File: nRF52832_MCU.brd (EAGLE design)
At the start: 43.2 x 22.1 mm, 27 parts, among them J100 DEBUG_CONNECTOR, U1 NRF52832, X1 32MHz, X2 32.768kHz

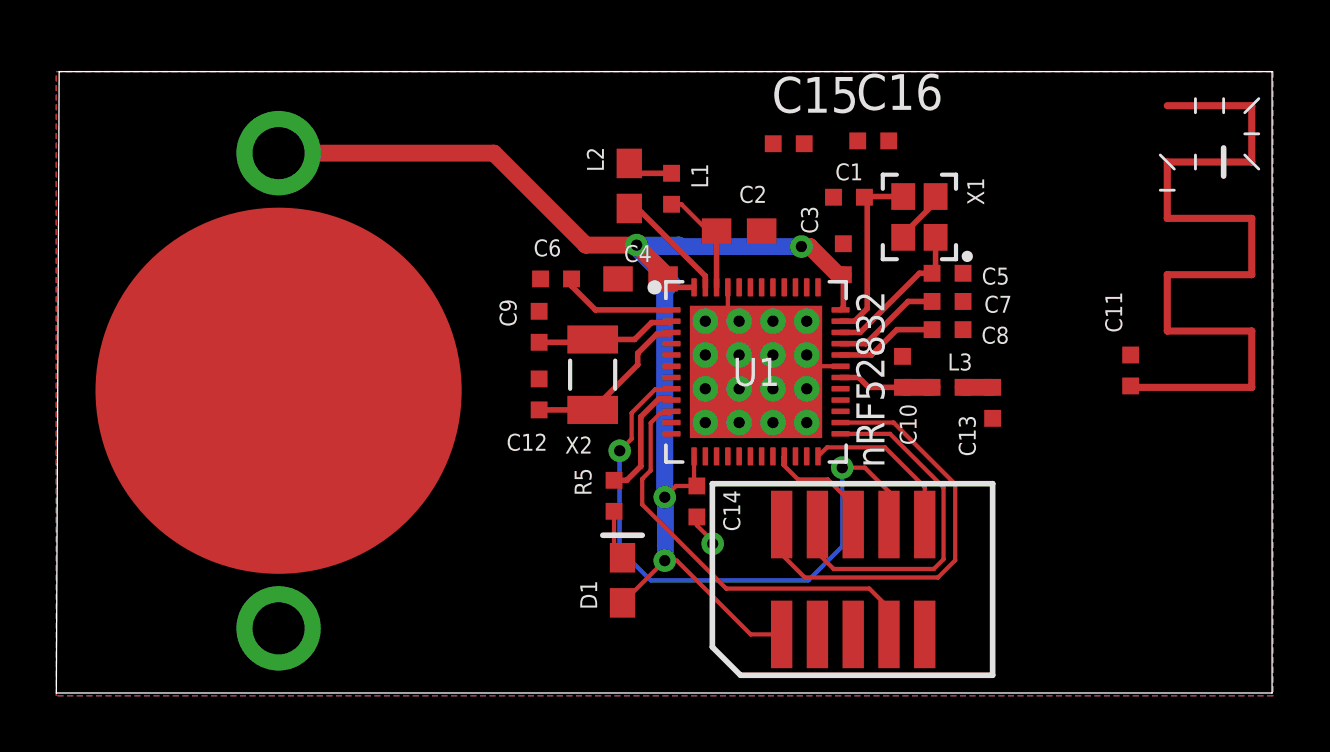
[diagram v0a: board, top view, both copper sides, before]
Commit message: Add missing capacitors
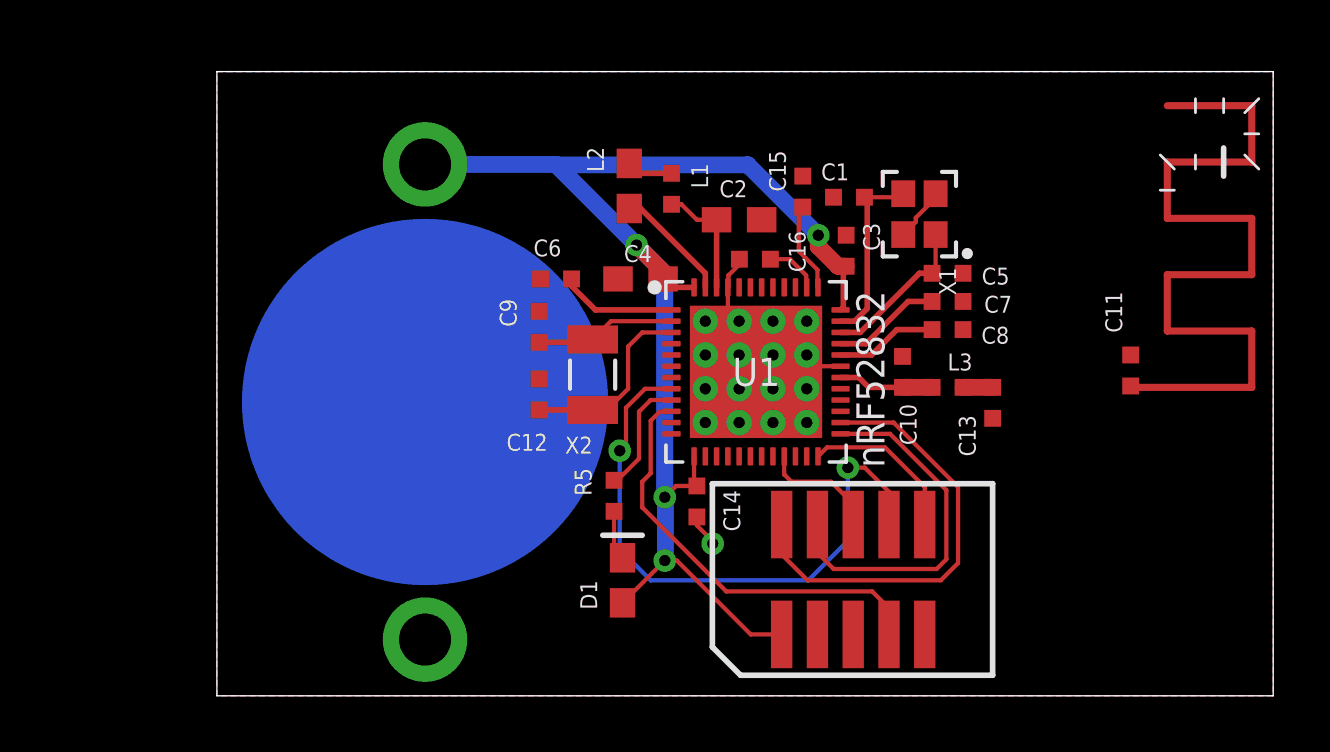
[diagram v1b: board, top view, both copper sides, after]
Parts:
- moved C16 5.94 mm to (37.3, 15.4), turned to 180 degrees
- moved BATT1 5.22 mm to (25.6, 10.3), flipped to the bottom
- moved C15 1.77 mm to (39.0, 17.8), turned to 90 degrees
- moved C2 0.40 mm to (36.7, 16.8)
- moved C3 0.32 mm to (40.5, 15.7)
- moved X1 0.10 mm to (43.1, 17.0)
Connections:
- removed net N$1: ANT1.P$1, C11.1
- net N$5: now also ANT1.P$1, C11.1
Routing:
- net P0.25: track 0.00 -> 3.19 mm
- net P0.26: track 0.00 -> 1.94 mm
- net VDD_P3V3: track 49.1 -> 50.6 mm
- net GND: track 7.28 -> 8.47 mm
- net XL2: track 6.08 -> 6.72 mm
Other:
- board size 43.2 x 22.1 mm -> 37.5 x 22.2 mm

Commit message: Update rastnest
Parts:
- moved C5 0.10 mm to (44.1, 15.0)
- moved C7 0.10 mm to (44.1, 14.0)
- moved C8 0.10 mm to (44.1, 13.0)
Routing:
- net VDD_P3V3: track 50.6 -> 47.1 mm
- net P0.06_TX: track 21.7 -> 20.2 mm

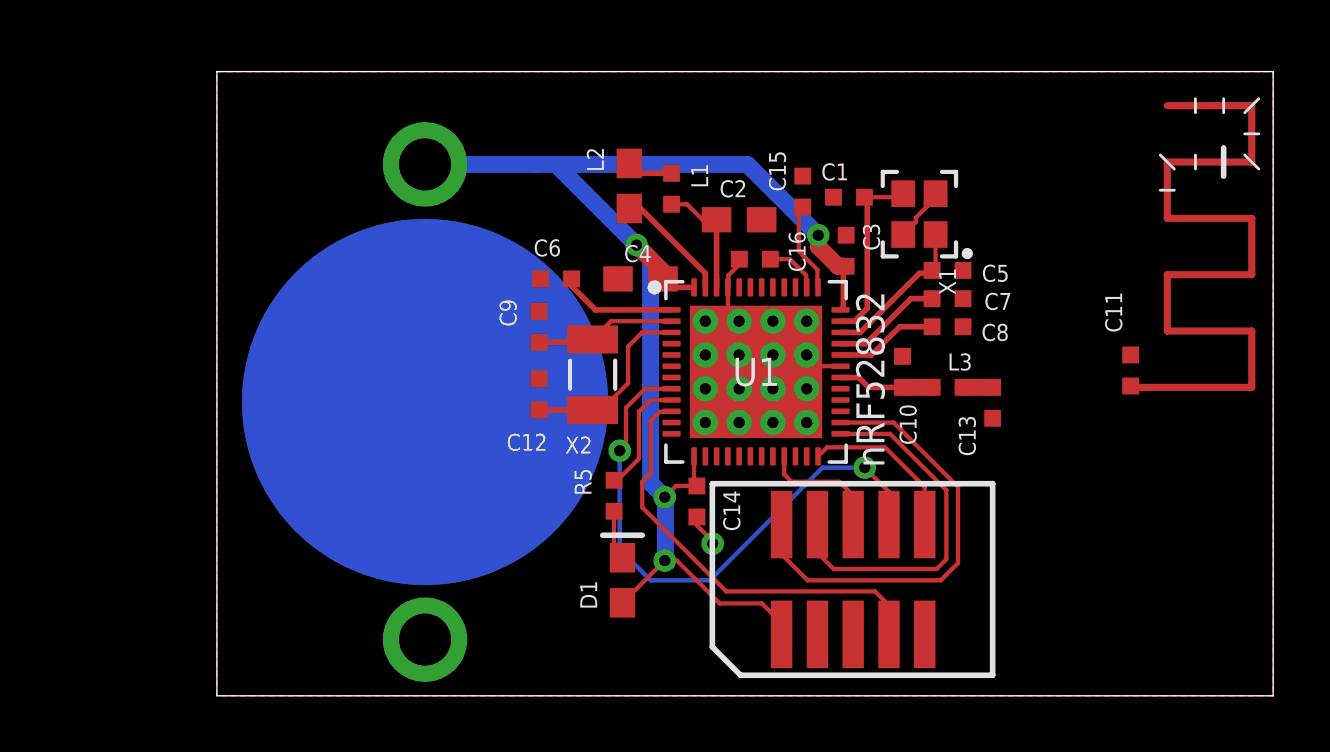
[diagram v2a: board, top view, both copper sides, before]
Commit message: Add additional pin connector
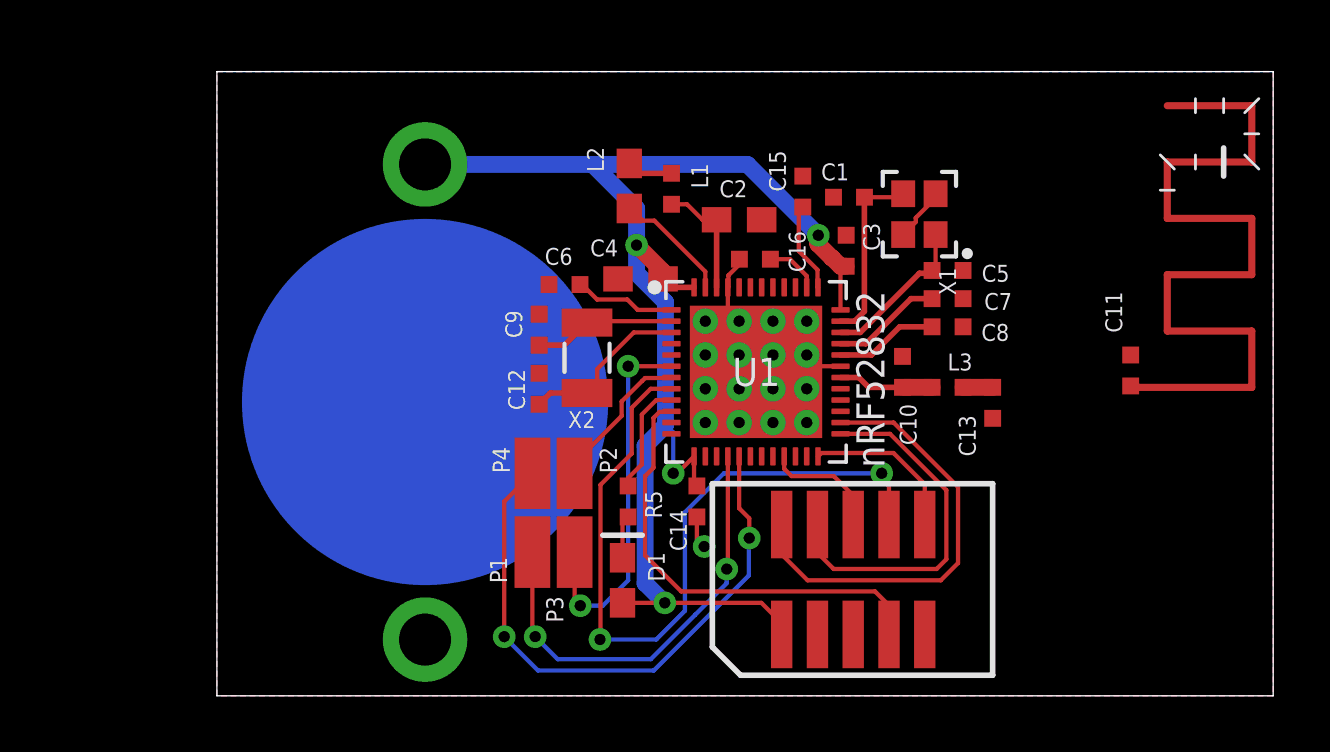
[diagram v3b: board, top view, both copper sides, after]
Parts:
- added P1, P2, P3, P4: WIREPADSMD1,27-254, wirepad:SMD1,27-2,54
- moved X2 0.63 mm to (31.3, 11.9)
- moved R5 0.54 mm to (32.8, 6.80)
- moved C6 0.36 mm to (30.5, 14.5)
- moved C12 0.20 mm to (29.6, 10.8)
- moved C9 0.10 mm to (29.6, 12.9)
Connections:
- net P0.04: now also P3.1
- net P0.05: now also P2.1
- net P0.13: now also P1.1
- net P0.14: now also P4.1
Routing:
- net P0.14: track 0.00 -> 21.2 mm, vias 0 -> 2
- net P0.13: track 0.00 -> 15.8 mm, vias 0 -> 2
- net P0.04: track 0.00 -> 13.2 mm, vias 0 -> 2
- net P0.06_TX: track 20.2 -> 26.8 mm
- net P0.05: track 0.00 -> 5.36 mm
- net VDD_P3V3: track 47.1 -> 48.6 mm
- net P0.08_RX: track 15.3 -> 16.2 mm
- net DEC1: track 4.15 -> 3.62 mm
